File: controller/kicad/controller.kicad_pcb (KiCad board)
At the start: 2 copper layers, 90 x 80 mm, 22 parts, among them J1 pcie_98, U1 ESD5344D, U10 ESD5344D, U11 WeAct_STM32H750_Module, U12 ESD5344D, U13 ESD5344D, U14 ESD5344D, U15 ESD5344D, U16 ESD5344D, U17 ESD5344D, U18 ESD5344D, U19 ESD5344D, U2 ESD5344D, U20 ESD5344D, U21 ESD5344D, U3 ESD5344D, U4 ESD5344D, U5 ESD5344D, U6 ESD5344D, U7 ESD5344D, U8 ESD5344D, U9 ESD5344D

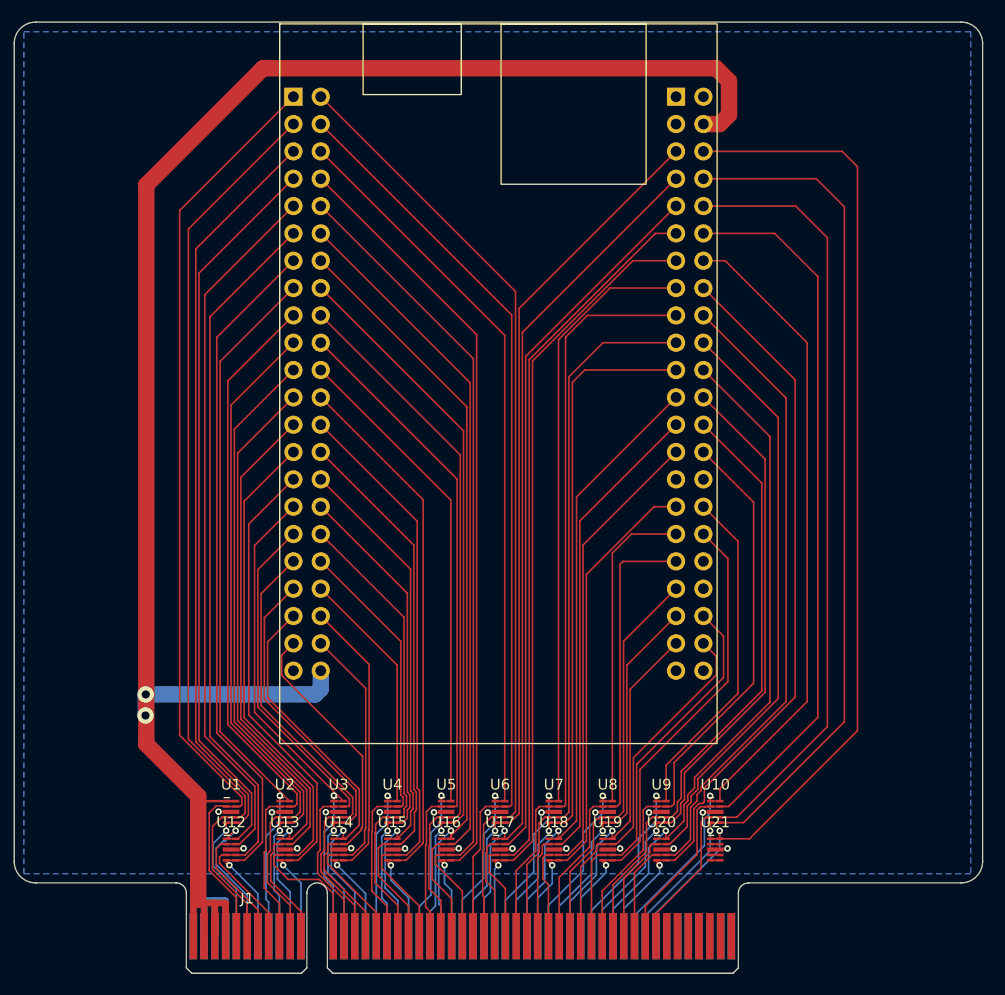
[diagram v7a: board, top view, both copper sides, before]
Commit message: Added to the controller boared 5V power arbitration.
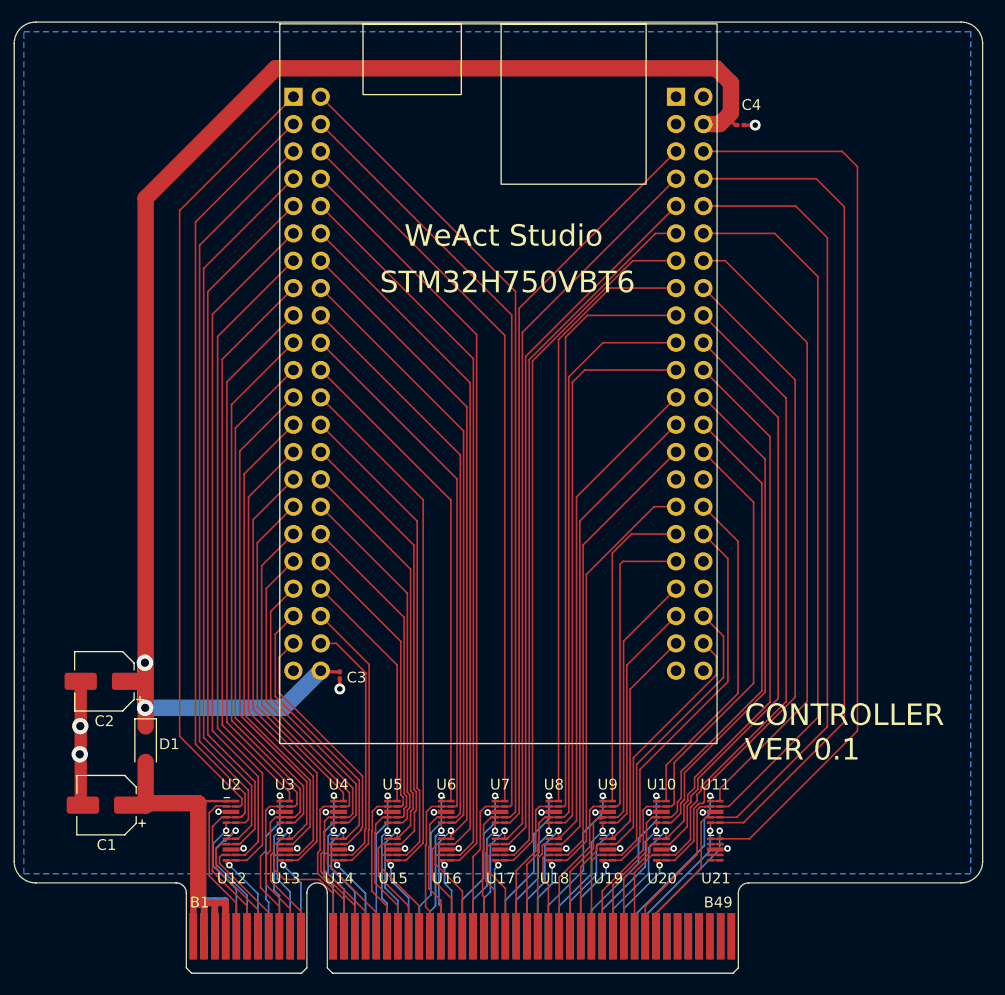
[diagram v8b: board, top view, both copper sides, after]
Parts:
- added C1: 100uf, Capacitor_SMD:CP_Elec_5x5.4, F.Cu at (50.4, 44.4)
- added C2: 100uf, Capacitor_SMD:CP_Elec_5x5.4, F.Cu at (50.2, 32.9)
- added C3: 1uf, Capacitor_SMD:C_0201_0603Metric, F.Cu at (72.1, 32.3)
- added C4: 1uf, Capacitor_SMD:C_0201_0603Metric, F.Cu at (109.3, -18.8)
- added D1: B5819W SL, Diode_SMD:D_SOD-123, F.Cu at (54.1, 38.7)
- renumbered U11 to U1, U9 to U10, U10 to U11, U1 to U2, U2 to U3, U3 to U4, U4 to U5, U5 to U6, U6 to U7, U7 to U8, U8 to U9
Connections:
- J1 pad B1: /+5V -> /+5VBUS
- J1 pad B2: /+5V -> /+5VBUS
- J1 pad B3: /+5V -> /+5VBUS
- J1 pad B4: /+5V -> /+5VBUS
- U2 pad 1: /+5V -> /+5VBUS
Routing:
- net /+5VBUS: track 0.00 -> 36.5 mm
- net /+5V: track 172.4 -> 139.9 mm
- net GND: track 43.3 -> 56.8 mm, vias 20 -> 24
- net /PE0: track 33.6 -> 34.4 mm
- net /PB9: track 38.8 -> 38.2 mm
- net /PB15: track 85.3 -> 84.8 mm
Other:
- board text added: "CONTROLLER VER 0.1"
- board text added: "STM32H750VBT6"
- board text added: "WeAct Studio"
